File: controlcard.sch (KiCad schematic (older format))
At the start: 1 part

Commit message: V0 schematic complete (?)
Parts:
- added D?: D_Schottky_x2_KCom_AKA, symbol D_Schottky_x2_KCom_AKA
- added P?: CONN_01X03, symbol CONN_01X03
- added P?: CONN_01X05, symbol CONN_01X05
- added P?: CONN_01X08, symbol CONN_01X08
- added Q? (x2): FDG1024NZ, SC-70-6, symbol FDG1024NZ
- added R?: 9.1R 2W, symbol R_Small
- added W? (x2): TEST_1P, symbol TEST_1P
- gave numbers to parts that had none: 1
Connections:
- net labels added: +15V, ADC_B2, ADC_B3, ADC_B7, IFB_A, IFB_B, IFB_BUS, IFB_C, MOTOR_TEMP, PWM_AH, PWM_AL, PWM_BH, PWM_BL, PWM_CH, PWM_CL, PWR_RDY, PWR_STG_TEMP, SCL/SYNCO, SDA/SYNCI, SPIA_MISO, SPIA_MOSI, SPIA_SCLK, VFB_A, VFB_B, VFB_BUS, VFB_C, Vds_A, Vds_B, Vds_C, ~FLT_DESAT, ~FLT_OTP, ~PWR_RESET, ~SPIA_CS
- wire segments 27 -> 66
- no-connect marks 0 -> 31
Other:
- note added: "+HV contactor and precharge relay"
- note added: "Todo: this contactor coil is a\nsignificant fraction of the +15V\nsupply current... better options?"
- moved on the sheet: J1

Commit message: Annotate, fix schematic DRC, footprint for DIMM100
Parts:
- gave numbers to parts that had none: 8
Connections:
- net SCL/SYNCO: now also J1.95 (GPIO_33)
- no-connect marks 31 -> 29
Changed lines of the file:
@@
 NoConn ~ 2700 5350
 NoConn ~ 2700 5550
-NoConn ~ 4700 5450
 NoConn ~ 4700 5350
 NoConn ~ 4700 5250
-NoConn ~ 4700 5050
 NoConn ~ 4700 4550
 NoConn ~ 4700 4450
@@
 	4700 4350 4950 4350
 $Comp
-L FDG1024NZ Q?
+L FDG1024NZ Q1
 U 1 1 57A7B53E
 P 6350 4900
-F 0 "Q?" H 6541 4991 50  0000 L CNN
+F 0 "Q1" H 6541 4991 50  0000 L CNN
 F 1 "FDG1024NZ" H 6541 4900 50  0000 L CNN
 F 2 "SC-70-6" H 6541 4809 50  0000 L CIN
@@
 $EndComp
 $Comp
-L FDG1024NZ Q?
+L FDG1024NZ Q1
 U 2 1 57A7B5D4
 P 7800 4900
-F 0 "Q?" H 7991 4991 50  0000 L CNN
+F 0 "Q1" H 7991 4991 50  0000 L CNN
 F 1 "FDG1024NZ" H 7991 4900 50  0000 L CNN
 F 2 "SC-70-6" H 7991 4809 50  0000 L CIN
@@
 $EndComp
 $Comp
-L GNDD #PWR?
+L GNDD #PWR011
 U 1 1 57A7B859
 P 6450 5100
-F 0 "#PWR?" H 6450 4850 50  0001 C CNN
+F 0 "#PWR011" H 6450 4850 50  0001 C CNN
 F 1 "GNDD" H 6450 4950 50  0000 C CNN
 F 2 "" H 6450 5100 50  0000 C CNN
@@
 $EndComp
 $Comp
-L GNDD #PWR?
+L GNDD #PWR012
 U 1 1 57A7B873
 P 7900 5100
-F 0 "#PWR?" H 7900 4850 50  0001 C CNN
+F 0 "#PWR012" H 7900 4850 50  0001 C CNN
 F 1 "GNDD" H 7900 4950 50  0000 C CNN
 F 2 "" H 7900 5100 50  0000 C CNN
@@
 	4700 4950 6150 4950
 $Comp
-L R_Small R?
+L R_Small R1
 U 1 1 57A7BAAF
 P 7250 3800
-F 0 "R?" H 7309 3846 50  0000 L CNN
+F 0 "R1" H 7309 3846 50  0000 L CNN
 F 1 "9.1R 2W" H 7309 3755 50  0000 L CNN
 F 2 "" H 7250 3800 50  0000 C CNN
@@
 Connection ~ 6450 4650
 $Comp
-L +15V #PWR?
+L +15V #PWR013
 U 1 1 57A7BE58
 P 7250 3700
-F 0 "#PWR?" H 7250 3550 50  0001 C CNN
+F 0 "#PWR013" H 7250 3550 50  0001 C CNN
 F 1 "+15V" H 7265 3873 50  0000 C CNN
 F 2 "" H 7250 3700 50  0000 C CNN
@@
 	7600 5350 7600 4950
 $Comp
-L CONN_01X03 P?
+L CONN_01X03 P3
 U 1 1 57A7D4A7
 P 8450 4550
-F 0 "P?" H 8528 4591 50  0000 L CNN
+F 0 "P3" H 8528 4591 50  0000 L CNN
 F 1 "CONN_01X03" H 8528 4500 50  0000 L CNN
 F 2 "" H 8450 4550 50  0000 C CNN
@@
 	6450 4550 8250 4550
 $Comp
-L D_Schottky_x2_KCom_AKA D?
+L D_Schottky_x2_KCom_AKA D1
 U 1 1 57A7D567
 P 7250 4200
-F 0 "D?" H 7250 4325 50  0000 C CNN
+F 0 "D1" H 7250 4325 50  0000 C CNN
 F 1 "D_Schottky_x2_KCom_AKA" H 7250 4415 50  0001 C CNN
 F 2 "" H 7250 4200 50  0000 C CNN
@@
 Connection ~ 7250 3950
 $Comp
-L CONN_01X05 P?
+L CONN_01X05 P1
 U 1 1 57A7DCAD
 P 1150 2250
-F 0 "P?" H 1069 1825 50  0000 C CNN
+F 0 "P1" H 1069 1825 50  0000 C CNN
 F 1 "CONN_01X05" H 1069 1916 50  0000 C CNN
 F 2 "" H 1150 2250 50  0000 C CNN
@@
 	1850 2250 1850 3050
 $Comp
-L GNDD #PWR?
+L GNDD #PWR014
 U 1 1 57A7DFB4
 P 1350 2600
-F 0 "#PWR?" H 1350 2350 50  0001 C CNN
+F 0 "#PWR014" H 1350 2350 50  0001 C CNN
 F 1 "GNDD" H 1350 2450 50  0000 C CNN
 F 2 "" H 1350 2600 50  0000 C CNN
@@
 	1350 2450 1350 2600
 $Comp
-L +5VD #PWR?
+L +5VD #PWR015
 U 1 1 57A7E048
 P 1350 2350
-F 0 "#PWR?" H 1350 2200 50  0001 C CNN
+F 0 "#PWR015" H 1350 2200 50  0001 C CNN
 F 1 "+5VD" H 1350 2490 50  0000 C CNN
 F 2 "" H 1350 2350 50  0000 C CNN
@@
 $EndComp
 $Comp
-L CONN_01X08 P?
+L CONN_01X08 P2
 U 1 1 57A7E1B2
 P 1200 5100
-F 0 "P?" H 1119 4525 50  0000 C CNN
+F 0 "P2" H 1119 4525 50  0000 C CNN
 F 1 "CONN_01X08" H 1119 4616 50  0000 C CNN
 F 2 "" H 1200 5100 50  0000 C CNN
@@
 $EndComp
 $Comp
-L GNDD #PWR?
+L GNDD #PWR016
 U 1 1 57A7E258
 P 1500 5550
-F 0 "#PWR?" H 1500 5300 50  0001 C CNN
+F 0 "#PWR016" H 1500 5300 50  0001 C CNN
 F 1 "GNDD" H 1500 5400 50  0000 C CNN
 F 2 "" H 1500 5550 50  0000 C CNN
@@
 	1500 5450 1500 5550
 $Comp
-L +5VD #PWR?
+L +5VD #PWR017
 U 1 1 57A7E36C
 P 1550 5350
-F 0 "#PWR?" H 1550 5200 50  0001 C CNN
+F 0 "#PWR017" H 1550 5200 50  0001 C CNN
 F 1 "+5VD" H 1550 5490 50  0000 C CNN
 F 2 "" H 1550 5350 50  0000 C CNN
@@
 	5400 4850 4700 4850
 $Comp
-L TEST_1P W?
+L TEST_1P W2
 U 1 1 57A7EB0A
 P 4700 2550
-F 0 "W?" V 4654 2738 50  0000 L CNN
+F 0 "W2" V 4654 2738 50  0000 L CNN
 F 1 "TEST_1P" V 4745 2738 50  0000 L CNN
 F 2 "" H 4900 2550 50  0000 C CNN
@@
 $EndComp
 $Comp
-L TEST_1P W?
+L TEST_1P W1
 U 1 1 57A7EC1F
 P 2700 2550
-F 0 "W?" V 2895 2624 50  0000 C CNN
+F 0 "W1" V 2895 2624 50  0000 C CNN
 F 1 "TEST_1P" V 2804 2624 50  0000 C CNN
 F 2 "" H 2900 2550 50  0000 C CNN
@@
 	0    -1   -1   0
 $EndComp
+Text Label 5450 5450 2    60   ~ 0
+SCL/SYNCO
+Wire Wire Line
+	4700 5450 5450 5450
 $EndSCHEMATC

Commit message: Footprints assigned, netlist generated - ready for layout
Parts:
- D1: footprint (none) -> TO_SOT_Packages_SMD:SOT-323
- J1: renamed from P1; footprint (none) -> Connectors_Molex:Connector_Molex_PicoBlade_53398-0571
- J2: renamed from P2; footprint (none) -> Connectors_Molex:Connector_Molex_PicoBlade_53398-0871
- J3: renamed from J1; footprint MODULE -> sictroller:5390213-1
- J4: renamed from P3; footprint (none) -> sictroller:Molex-SL-3POS-RA
- Q1: footprint SC-70-6 -> TO_SOT_Packages_SMD:SC-70-6
- R1: footprint (none) -> Resistors_ThroughHole:Resistor_Horizontal_RM15mm
- W1, W2: footprint (none) -> Measurement_Points:Measurement_Point_Round-SMD-Pad_Small
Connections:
- net +15V: now also D1.2 (K)
- net at J4.1 (P1), R1.2: no longer D1.2 (K)
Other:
- note added: "Todo: this contactor coil eats a\nsignificant fraction of the +15V\nsupply current... better options?"
- note removed: "Todo: this contactor coil is a\nsignificant fraction of the +15V\nsupply current... better options?"
- moved on the sheet: R1
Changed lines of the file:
@@
 $EndComp
 $Comp
-L TMDSCNCD28069 J1
+L TMDSCNCD28069 J3
 U 1 1 57A180A1
 P 3700 3650
-F 0 "J1" H 3050 1500 50  0000 C CNN
+F 0 "J3" H 3050 1500 50  0000 C CNN
 F 1 "TMDSCNCD28069" H 4050 1500 50  0000 C CNN
-F 2 "MODULE" H 3700 3650 50  0001 C CNN
+F 2 "sictroller:5390213-1" H 3700 3650 50  0001 C CNN
 F 3 "DOCUMENTATION" H 3700 3550 50  0001 C CNN
 	1    3700 3650
@@
 F 0 "Q1" H 6541 4991 50  0000 L CNN
 F 1 "FDG1024NZ" H 6541 4900 50  0000 L CNN
-F 2 "SC-70-6" H 6541 4809 50  0000 L CIN
+F 2 "TO_SOT_Packages_SMD:SC-70-6" H 6541 4809 50  0000 L CIN
 F 3 "" H 6350 4900 50  0000 L CNN
 	1    6350 4900
@@
 F 0 "Q1" H 7991 4991 50  0000 L CNN
 F 1 "FDG1024NZ" H 7991 4900 50  0000 L CNN
-F 2 "SC-70-6" H 7991 4809 50  0000 L CIN
+F 2 "TO_SOT_Packages_SMD:SC-70-6" H 7991 4809 50  0000 L CIN
 F 3 "" H 7800 4900 50  0000 L CNN
 	2    7800 4900
@@
 L R_Small R1
 U 1 1 57A7BAAF
-P 7250 3800
-F 0 "R1" H 7309 3846 50  0000 L CNN
-F 1 "9.1R 2W" H 7309 3755 50  0000 L CNN
-F 2 "" H 7250 3800 50  0000 C CNN
-F 3 "" H 7250 3800 50  0000 C CNN
-	1    7250 3800
+P 8250 4200
+F 0 "R1" H 8309 4246 50  0000 L CNN
+F 1 "9.1R 2W" H 8309 4155 50  0000 L CNN
+F 2 "Resistors_ThroughHole:Resistor_Horizontal_RM15mm" H 8250 4200 50  0001 C CNN
+F 3 "" H 8250 4200 50  0000 C CNN
+	1    8250 4200
 	1    0    0    -1
 $EndComp
@@
 L +15V #PWR013
 U 1 1 57A7BE58
-P 7250 3700
-F 0 "#PWR013" H 7250 3550 50  0001 C CNN
-F 1 "+15V" H 7265 3873 50  0000 C CNN
-F 2 "" H 7250 3700 50  0000 C CNN
-F 3 "" H 7250 3700 50  0000 C CNN
-	1    7250 3700
+P 7750 3900
+F 0 "#PWR013" H 7750 3750 50  0001 C CNN
+F 1 "+15V" H 7765 4073 50  0000 C CNN
+F 2 "" H 7750 3900 50  0000 C CNN
+F 3 "" H 7750 3900 50  0000 C CNN
+	1    7750 3900
 	1    0    0    -1
 $EndComp
 Text Notes 6550 5750 0    60   ~ 0
-Todo: this contactor coil is a\nsignificant fraction of the +15V\nsupply current... better options?
-Text Notes 6450 3400 0    60   ~ 0
+Todo: this contactor coil eats a\nsignificant fraction of the +15V\nsupply current... better options?
+Text Notes 6650 3550 0    60   ~ 0
 +HV contactor and precharge relay
 Wire Wire Line
@@
 	7600 5350 7600 4950
 $Comp
-L CONN_01X03 P3
+L CONN_01X03 J4
 U 1 1 57A7D4A7
 P 8450 4550
-F 0 "P3" H 8528 4591 50  0000 L CNN
+F 0 "J4" H 8528 4591 50  0000 L CNN
 F 1 "CONN_01X03" H 8528 4500 50  0000 L CNN
-F 2 "" H 8450 4550 50  0000 C CNN
+F 2 "sictroller:Molex-SL-3POS-RA" H 8450 4550 50  0001 C CNN
 F 3 "" H 8450 4550 50  0000 C CNN
 	1    8450 4550
@@
 F 0 "D1" H 7250 4325 50  0000 C CNN
 F 1 "D_Schottky_x2_KCom_AKA" H 7250 4415 50  0001 C CNN
-F 2 "" H 7250 4200 50  0000 C CNN
+F 2 "TO_SOT_Packages_SMD:SOT-323" H 7250 4200 50  0001 C CNN
 F 3 "" H 7250 4200 50  0000 C CNN
 	1    7250 4200
@@
 	7900 4700 7900 4650
 Connection ~ 7900 4650
-Wire Wire Line
-	7250 3900 7250 4000
-Wire Wire Line
-	7250 3950 8250 3950
-Wire Wire Line
-	8250 3950 8250 4450
-Connection ~ 7250 3950
-$Comp
-L CONN_01X05 P1
+$Comp
+L CONN_01X05 J1
 U 1 1 57A7DCAD
 P 1150 2250
-F 0 "P1" H 1069 1825 50  0000 C CNN
+F 0 "J1" H 1069 1825 50  0000 C CNN
 F 1 "CONN_01X05" H 1069 1916 50  0000 C CNN
-F 2 "" H 1150 2250 50  0000 C CNN
+F 2 "Connectors_Molex:Connector_Molex_PicoBlade_53398-0571" H 1150 2250 50  0001 C CNN
 F 3 "" H 1150 2250 50  0000 C CNN
 	1    1150 2250
@@
 $EndComp
 $Comp
-L CONN_01X08 P2
+L CONN_01X08 J2
 U 1 1 57A7E1B2
 P 1200 5100
-F 0 "P2" H 1119 4525 50  0000 C CNN
+F 0 "J2" H 1119 4525 50  0000 C CNN
 F 1 "CONN_01X08" H 1119 4616 50  0000 C CNN
-F 2 "" H 1200 5100 50  0000 C CNN
+F 2 "Connectors_Molex:Connector_Molex_PicoBlade_53398-0871" H 1200 5100 50  0001 C CNN
 F 3 "" H 1200 5100 50  0000 C CNN
 	1    1200 5100
@@
 F 0 "W2" V 4654 2738 50  0000 L CNN
 F 1 "TEST_1P" V 4745 2738 50  0000 L CNN
-F 2 "" H 4900 2550 50  0000 C CNN
+F 2 "Measurement_Points:Measurement_Point_Round-SMD-Pad_Small" H 4900 2550 50  0001 C CNN
 F 3 "" H 4900 2550 50  0000 C CNN
 	1    4700 2550
@@
 F 0 "W1" V 2895 2624 50  0000 C CNN
 F 1 "TEST_1P" V 2804 2624 50  0000 C CNN
-F 2 "" H 2900 2550 50  0000 C CNN
+F 2 "Measurement_Points:Measurement_Point_Round-SMD-Pad_Small" H 2900 2550 50  0001 C CNN
 F 3 "" H 2900 2550 50  0000 C CNN
 	1    2700 2550
@@
 Wire Wire Line
 	4700 5450 5450 5450
+Wire Wire Line
+	8250 4300 8250 4450
+Wire Wire Line
+	8250 4100 8250 4000
+Wire Wire Line
+	8250 4000 7250 4000
+Wire Wire Line
+	7750 3900 7750 4000
+Connection ~ 7750 4000
 $EndSCHEMATC

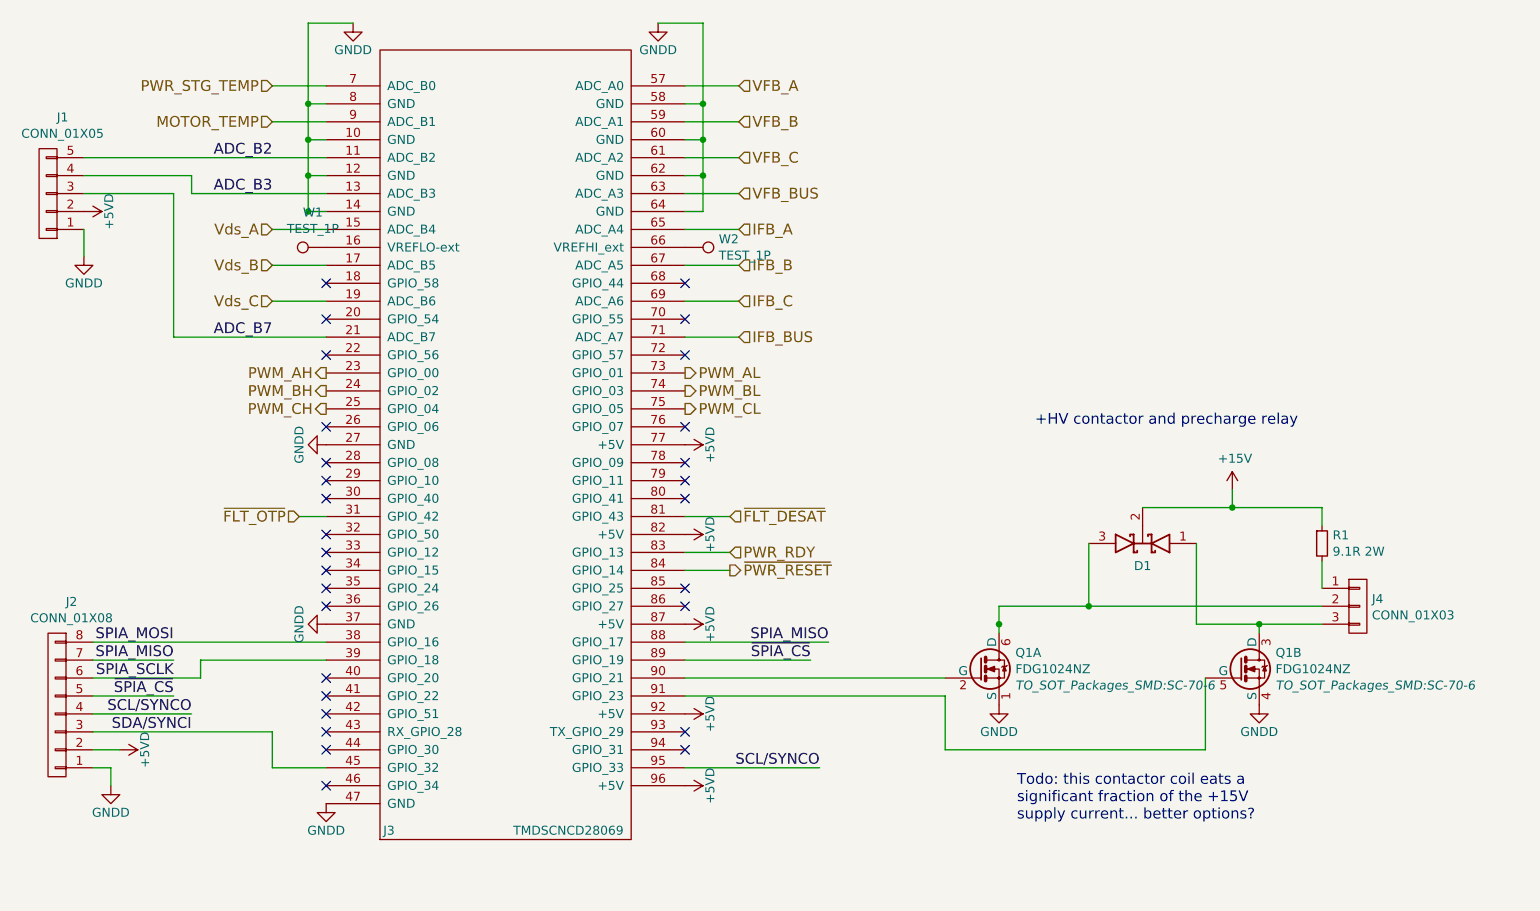
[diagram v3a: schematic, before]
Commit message: More aux pins, SKUs for some components
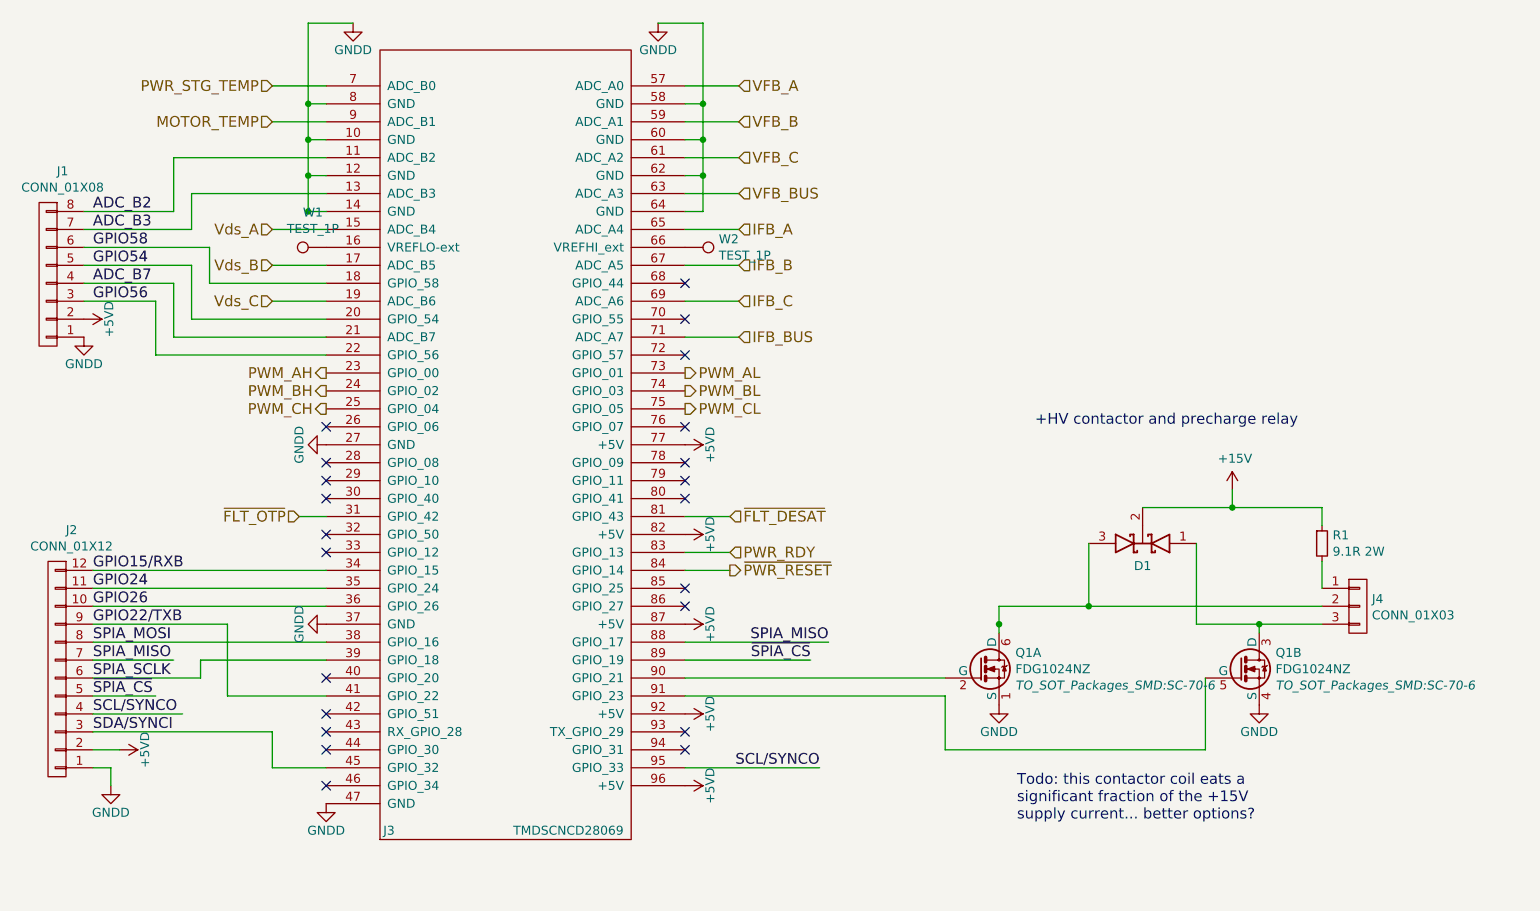
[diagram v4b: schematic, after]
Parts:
- removed J1: CONN_01X05, Connectors_Molex:Connector_Molex_PicoBlade_53398-0571, symbol CONN_01X05
- removed J2: CONN_01X08, Connectors_Molex:Connector_Molex_PicoBlade_53398-0871, symbol CONN_01X08
- added J1: CONN_01X08, Connectors_Molex:Connector_Molex_PicoBlade_53398-0871, symbol CONN_01X08
- added J2: CONN_01X12, Connectors_Molex:Connector_Molex_PicoBlade_53398-1271, symbol CONN_01X12
- D1: SKU (none) -> 497-5550-1-ND; Supplier (none) -> Digikey
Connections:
- net labels added: GPIO15/RXB, GPIO22/TXB, GPIO24, GPIO26, GPIO54, GPIO56, GPIO58
- wire segments 68 -> 84
- no-connect marks 29 -> 22

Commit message: Add test points; PCB connectors placed
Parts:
- J1: footprint Connectors_Molex:Connector_Molex_PicoBlade_53398-0871 -> Connectors_Molex:Connector_Molex_PicoBlade_53261-0871
- J2: footprint Connectors_Molex:Connector_Molex_PicoBlade_53398-1271 -> Connectors_Molex:Connector_Molex_PicoBlade_53261-1271
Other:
- note added: "GPIO31, 34 drive red LEDs on the controlcard"
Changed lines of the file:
@@
 $EndDescr
 $Comp
-L +5VD #PWR01
+L +5VD #PWR15
 U 1 1 57A1808F
 P 4700 4150
-F 0 "#PWR01" H 4700 4000 50  0001 C CNN
+F 0 "#PWR15" H 4700 4000 50  0001 C CNN
 F 1 "+5VD" H 4700 4290 50  0000 C CNN
 F 2 "" H 4700 4150 50  0000 C CNN
@@
 $EndComp
 $Comp
-L +5VD #PWR02
+L +5VD #PWR17
 U 1 1 57A18095
 P 4700 5150
-F 0 "#PWR02" H 4700 5000 50  0001 C CNN
+F 0 "#PWR17" H 4700 5000 50  0001 C CNN
 F 1 "+5VD" H 4700 5290 50  0000 C CNN
 F 2 "" H 4700 5150 50  0000 C CNN
@@
 $EndComp
 $Comp
-L GNDD #PWR03
+L GNDD #PWR13
 U 1 1 57A1809B
 P 4550 1300
-F 0 "#PWR03" H 4550 1050 50  0001 C CNN
+F 0 "#PWR13" H 4550 1050 50  0001 C CNN
 F 1 "GNDD" H 4550 1150 50  0000 C CNN
 F 2 "" H 4550 1300 50  0000 C CNN
@@
 $EndComp
 $Comp
-L +5VD #PWR04
+L +5VD #PWR16
 U 1 1 57A180A8
 P 4700 4650
-F 0 "#PWR04" H 4700 4500 50  0001 C CNN
+F 0 "#PWR16" H 4700 4500 50  0001 C CNN
 F 1 "+5VD" H 4700 4790 50  0000 C CNN
 F 2 "" H 4700 4650 50  0000 C CNN
@@
 $EndComp
 $Comp
-L +5VD #PWR05
+L +5VD #PWR18
 U 1 1 57A180AE
 P 4700 5550
-F 0 "#PWR05" H 4700 5400 50  0001 C CNN
+F 0 "#PWR18" H 4700 5400 50  0001 C CNN
 F 1 "+5VD" H 4700 5690 50  0000 C CNN
 F 2 "" H 4700 5550 50  0000 C CNN
@@
 $EndComp
 $Comp
-L GNDD #PWR06
+L GNDD #PWR11
 U 1 1 57A180B4
 P 2700 5650
-F 0 "#PWR06" H 2700 5400 50  0001 C CNN
+F 0 "#PWR11" H 2700 5400 50  0001 C CNN
 F 1 "GNDD" H 2700 5500 50  0000 C CNN
 F 2 "" H 2700 5650 50  0000 C CNN
@@
 $EndComp
 $Comp
-L GNDD #PWR07
+L GNDD #PWR10
 U 1 1 57A180BA
 P 2700 4650
-F 0 "#PWR07" H 2700 4400 50  0001 C CNN
+F 0 "#PWR10" H 2700 4400 50  0001 C CNN
 F 1 "GNDD" H 2700 4500 50  0000 C CNN
 F 2 "" H 2700 4650 50  0000 C CNN
@@
 $EndComp
 $Comp
-L +5VD #PWR08
+L +5VD #PWR14
 U 1 1 57A180E0
 P 4700 3650
-F 0 "#PWR08" H 4700 3500 50  0001 C CNN
+F 0 "#PWR14" H 4700 3500 50  0001 C CNN
 F 1 "+5VD" H 4700 3790 50  0000 C CNN
 F 2 "" H 4700 3650 50  0000 C CNN
@@
 $EndComp
 $Comp
-L GNDD #PWR09
+L GNDD #PWR12
 U 1 1 57A180E7
 P 2850 1300
-F 0 "#PWR09" H 2850 1050 50  0001 C CNN
+F 0 "#PWR12" H 2850 1050 50  0001 C CNN
 F 1 "GNDD" H 2850 1150 50  0000 C CNN
 F 2 "" H 2850 1300 50  0000 C CNN
@@
 $EndComp
 $Comp
-L GNDD #PWR010
+L GNDD #PWR9
 U 1 1 57A180ED
 P 2700 3650
-F 0 "#PWR010" H 2700 3400 50  0001 C CNN
+F 0 "#PWR9" H 2700 3400 50  0001 C CNN
 F 1 "GNDD" H 2700 3500 50  0000 C CNN
 F 2 "" H 2700 3650 50  0000 C CNN
@@
 $EndComp
 $Comp
-L GNDD #PWR011
+L GNDD #PWR19
 U 1 1 57A7B859
 P 6450 5100
-F 0 "#PWR011" H 6450 4850 50  0001 C CNN
+F 0 "#PWR19" H 6450 4850 50  0001 C CNN
 F 1 "GNDD" H 6450 4950 50  0000 C CNN
 F 2 "" H 6450 5100 50  0000 C CNN
@@
 $EndComp
 $Comp
-L GNDD #PWR012
+L GNDD #PWR21
 U 1 1 57A7B873
 P 7900 5100
-F 0 "#PWR012" H 7900 4850 50  0001 C CNN
+F 0 "#PWR21" H 7900 4850 50  0001 C CNN
 F 1 "GNDD" H 7900 4950 50  0000 C CNN
 F 2 "" H 7900 5100 50  0000 C CNN
@@
 $EndComp
 $Comp
-L +15V #PWR013
+L +15V #PWR20
 U 1 1 57A7BE58
 P 7750 3900
-F 0 "#PWR013" H 7750 3750 50  0001 C CNN
+F 0 "#PWR20" H 7750 3750 50  0001 C CNN
 F 1 "+15V" H 7765 4073 50  0000 C CNN
 F 2 "" H 7750 3900 50  0000 C CNN
@@
 $EndComp
 $Comp
-L GNDD #PWR014
+L GNDD #PWR6
 U 1 1 57A7DFB4
 P 1350 3050
-F 0 "#PWR014" H 1350 2800 50  0001 C CNN
+F 0 "#PWR6" H 1350 2800 50  0001 C CNN
 F 1 "GNDD" H 1350 2900 50  0000 C CNN
 F 2 "" H 1350 3050 50  0000 C CNN
@@
 $EndComp
 $Comp
-L +5VD #PWR015
+L +5VD #PWR5
 U 1 1 57A7E048
 P 1350 2950
-F 0 "#PWR015" H 1350 2800 50  0001 C CNN
+F 0 "#PWR5" H 1350 2800 50  0001 C CNN
 F 1 "+5VD" H 1350 3090 50  0000 C CNN
 F 2 "" H 1350 2950 50  0000 C CNN
@@
 $EndComp
 $Comp
-L GNDD #PWR016
+L GNDD #PWR7
 U 1 1 57A7E258
 P 1500 5550
-F 0 "#PWR016" H 1500 5300 50  0001 C CNN
+F 0 "#PWR7" H 1500 5300 50  0001 C CNN
 F 1 "GNDD" H 1500 5400 50  0000 C CNN
 F 2 "" H 1500 5550 50  0000 C CNN
@@
 $EndComp
 $Comp
-L +5VD #PWR017
+L +5VD #PWR8
 U 1 1 57A7E36C
 P 1550 5350
-F 0 "#PWR017" H 1550 5200 50  0001 C CNN
+F 0 "#PWR8" H 1550 5200 50  0001 C CNN
 F 1 "+5VD" H 1550 5490 50  0000 C CNN
 F 2 "" H 1550 5350 50  0000 C CNN
@@
 F 0 "J1" H 1069 2125 50  0000 C CNN
 F 1 "CONN_01X08" H 1069 2216 50  0000 C CNN
-F 2 "Connectors_Molex:Connector_Molex_PicoBlade_53398-0871" H 1150 2700 50  0001 C CNN
+F 2 "Connectors_Molex:Connector_Molex_PicoBlade_53261-0871" H 1150 2700 50  0001 C CNN
 F 3 "" H 1150 2700 50  0000 C CNN
 	1    1150 2700
@@
 F 0 "J2" H 1119 4125 50  0000 C CNN
 F 1 "CONN_01X12" H 1119 4216 50  0000 C CNN
-F 2 "Connectors_Molex:Connector_Molex_PicoBlade_53398-1271" H 1200 4900 50  0001 C CNN
+F 2 "Connectors_Molex:Connector_Molex_PicoBlade_53261-1271" H 1200 4900 50  0001 C CNN
 F 3 "" H 1200 4900 50  0000 C CNN
 	1    1200 4900
@@
 	1    0    0    -1
 $EndComp
+Text Notes 2650 6150 0    60   ~ 0
+GPIO31, 34 drive red LEDs on the controlcard
 $EndSCHEMATC

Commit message: Delete Vds FB
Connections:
- net labels removed: Vds_A, Vds_B, Vds_C
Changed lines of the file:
@@
 Text HLabel 5000 3050 2    60   Input ~ 0
 IFB_BUS
-Text HLabel 2400 2450 0    60   Input ~ 0
-Vds_A
-Text HLabel 2400 2650 0    60   Input ~ 0
-Vds_B
-Text HLabel 2400 2850 0    60   Input ~ 0
-Vds_C
 Text HLabel 2700 3250 0    60   Output ~ 0
 PWM_AH
